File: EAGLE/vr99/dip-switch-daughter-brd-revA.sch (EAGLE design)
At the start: 9 parts

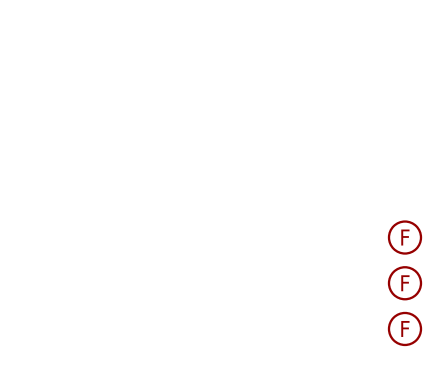
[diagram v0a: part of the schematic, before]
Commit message: DIP Switch DB
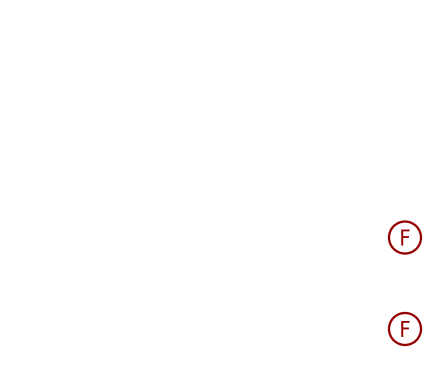
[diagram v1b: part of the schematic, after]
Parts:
- removed U$1: FIDUCIAL, __temp_to_delete:FIDUCIAL
- renumbered U$2 to F2, U$7 to F1
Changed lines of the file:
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@@
 <part name="JDIP1" library="molex-pico-ezmate" deviceset="MOLEX_0781710006" device=""/>
 <part name="SUPPLY67" library="supply2" library_urn="urn:adsk.eagle:library:372" deviceset="GND" device=""/>
-<part name="U$7" library="__temp_to_delete" deviceset="FIDUCIAL" device=""/>
+<part name="F1" library="__temp_to_delete" deviceset="FIDUCIAL" device=""/>
 <part name="D1" library="jlcpcb_basic_parts" deviceset="1N5819WS" device=""/>
 <part name="FRAME1" library="frames" library_urn="urn:adsk.eagle:library:229" deviceset="DINA5_L" device=""/>
-<part name="U$1" library="__temp_to_delete" deviceset="FIDUCIAL" device=""/>
 <part name="D2" library="jlcpcb_basic_parts" deviceset="1N5819WS" device=""/>
 <part name="D3" library="jlcpcb_basic_parts" deviceset="1N5819WS" device=""/>
 <part name="D4" library="jlcpcb_basic_parts" deviceset="1N5819WS" device=""/>
 <part name="DIP-SWITCH" library="untitled" deviceset="DIP004" device=""/>
-<part name="U$2" library="__temp_to_delete" deviceset="FIDUCIAL" device=""/>
+<part name="F2" library="__temp_to_delete" deviceset="FIDUCIAL" device=""/>
 </parts>
 <sheets>
@@
 <attribute name="VALUE" x="76.835" y="62.865" size="1.778" layer="96"/>
 </instance>
-<instance part="U$7" gate="G$1" x="134.62" y="20.32" smashed="yes"/>
+<instance part="F1" gate="G$1" x="134.62" y="20.32" smashed="yes"/>
 <instance part="D1" gate="G$1" x="104.14" y="71.12" smashed="yes" rot="R270">
 <attribute name="NAME" x="106.045" y="73.406" size="1.778" layer="95" rot="R270"/>
@@
 <attribute name="SHEET" x="154.305" y="5.08" size="2.54" layer="94"/>
 </instance>
-<instance part="U$1" gate="G$1" x="134.62" y="15.24" smashed="yes"/>
 <instance part="D2" gate="G$1" x="111.76" y="71.12" smashed="yes" rot="R270">
 <attribute name="NAME" x="113.665" y="73.406" size="1.778" layer="95" rot="R270"/>
@@
 <attribute name="VALUE" x="91.44" y="71.755" size="1.778" layer="96"/>
 </instance>
-<instance part="U$2" gate="G$1" x="134.62" y="10.16" smashed="yes"/>
+<instance part="F2" gate="G$1" x="134.62" y="10.16" smashed="yes"/>
 </instances>
 <busses>
